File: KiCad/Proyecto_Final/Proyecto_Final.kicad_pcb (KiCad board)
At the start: 2 copper layers, 240 parts, among them J1 RF_IN, J10 PF, J11 PB, J12 PE, J13 PA, J14 PD, J15 SPI4, J16 CLK_SEL, J17 CTRL_MODE, J2 ADC_CLK_SEL, J3 5v, J4 I2C1, J5 ARM SWD, J6 USB_B_Micro, J7 Boot_Select, J8 PG, J9 PC, Q1 BSS315P, SW1 Reset, T1 B0310J50100AHF, T2 B0310J50100AHF, T3 2450BL05A0100, U1 SKY13351, U10 MAX2837, U11 TLV1117-33, U12 TPD4S012DRYR, U13 STM32F723ZCTx, U14 5P49V6975, U2 RFFC5072, U3 SKY13351, U4 SKY13351, U5 SKY13351, U6 SKY13351, U7 SKY13351, U8 MAAL-010200, U9 MAX1193ETI+, Y1 25MHz

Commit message: Avance PCB.
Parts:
- removed the R12 at (155.5, 47.4)
- removed the R13 at (158.4, 44.3)
- removed the R14 at (176.4, 60.3)
- removed the R15 at (152.6, 49.4)
- added R2: 10k, Resistor_SMD:R_0402_1005Metric, F.Cu at (78.7, 63.5)
- J16: value CLK_SEL -> CFG_SEL
- moved FB1 100.4 mm to (211.3, 86.4)
- moved D2 98.0 mm to (193.0, 115.6)
- moved L4 96.4 mm to (119.9, 131.3), turned to 270 degrees
- moved C58 95.9 mm to (118.3, 131.8), turned to 180 degrees
- moved C56 85.7 mm to (118.3, 130.9), turned to 180 degrees
- moved C2 74.1 mm to (105.7, 137.4), turned to 180 degrees
- moved C3 69.3 mm to (105.6, 128.7)
- moved C10 68.4 mm to (110.4, 129.5), turned to 270 degrees
- moved C8 68.1 mm to (102.9, 137.1), turned to 180 degrees
- moved C11 66.3 mm to (114.4, 131.6), turned to 180 degrees
- moved C4 62.2 mm to (105.6, 127.7)
- moved C1 61.9 mm to (105.7, 136.4), turned to 180 degrees
- moved C5 60.4 mm to (115.3, 129.5), turned to 90 degrees
- moved J17 60.2 mm to (113.0, 99.1)
- moved U1 59.9 mm to (113.9, 129.0), turned to 270 degrees
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- renumbered C14 to C13, C15 to C14, C16 to C15, C17 to C16, C13 to C17, R9 to R10, R10 to R11, R11 to R12, R16 to R13, R17 to R14, R18 to R15, R19 to R16, R20 to R17, R21 to R18, R22 to R19, R23 to R20, R24 to R21, R25 to R22, R34 to R23, R35 to R24, R26 to R25, R27 to R26, R28 to R27, R29 to R28, R30 to R29, R2 to R3, R31 to R30, R32 to R31, R33 to R32, R3 to R4, R4 to R5, R5 to R6, R6 to R7, R7 to R8, R8 to R9
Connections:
- net Net-(C56-Pad1) renamed /Transceptor/RXRF+
- net Net-(C58-Pad1) renamed /Transceptor/RXRF-
- net Net-(L1-Pad2) renamed /Frontend_analog/MIX_OPP
- net Net-(L2-Pad2) renamed /Frontend_analog/MIX_OPN
- T2 pad 3: MIX_IPP -> MIX_IPN
- T2 pad 4: MIX_IPN -> MIX_IPP
- T3 pad 3: Net-(C56-Pad2) -> Net-(C58-Pad2)
- T3 pad 4: Net-(C58-Pad2) -> Net-(C56-Pad2)
- U1 pad 1: Net-(C10-Pad1) -> SWITCH
- U1 pad 3: SWITCH -> Net-(C10-Pad1)
- U9 pad 1: _INA- -> INA-
- U9 pad 2: _INA+ -> INA+
- U9 pad 6: _INB+ -> INB+
- U9 pad 7: _INB- -> INB-
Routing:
- net GND: track 0.00 -> 9.33 mm, vias 0 -> 9
- net +3.3VA: track 0.00 -> 7.93 mm, vias 0 -> 2
- net /Frontend_analog/MIX_OPN: track 0.00 -> 6.96 mm
- net /Frontend_analog/MIX_OPP: track 0.00 -> 6.59 mm, vias 0 -> 2
- net Net-(C10-Pad1): track 0.00 -> 4.27 mm
- net /Transceptor/RXRF+: track 0.00 -> 4.11 mm
- net /Transceptor/RXRF-: track 0.00 -> 4.11 mm
- net VDD: track 0.00 -> 3.82 mm, vias 0 -> 1
- net SWITCH: track 0.00 -> 3.75 mm
- net Net-(C11-Pad2): track 0.00 -> 2.16 mm
- net Net-(C10-Pad2): track 0.00 -> 1.38 mm
- net Rx_Mix: track 0.00 -> 1.30 mm
- net Net-(C58-Pad2): track 0.00 -> 1.30 mm
- net Net-(C56-Pad2): track 0.00 -> 1.29 mm
- net Rx_Mix_Bypass: track 0.00 -> 1.23 mm
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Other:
- copper layers 2 -> 4
- net class 100 Ohms Diferencial added: clearance 0.1, trace_width 0.25, via_dia 0.6, via_drill 0.3
- net class 50 Ohms Unico added: clearance 0.1, trace_width 0.3, via_dia 0.6, via_drill 0.3
- net class 90 Ohms Diferencial added: clearance 0.1, trace_width 0.25, via_dia 0.6, via_drill 0.3
- net class Default: clearance 0.2 -> 0.1
- rule trace_clearance: 0.2 -> 0.1
- rule via_min_drill: 0.3 -> 0.2
- rule via_min_size: 0.4 -> 0.45

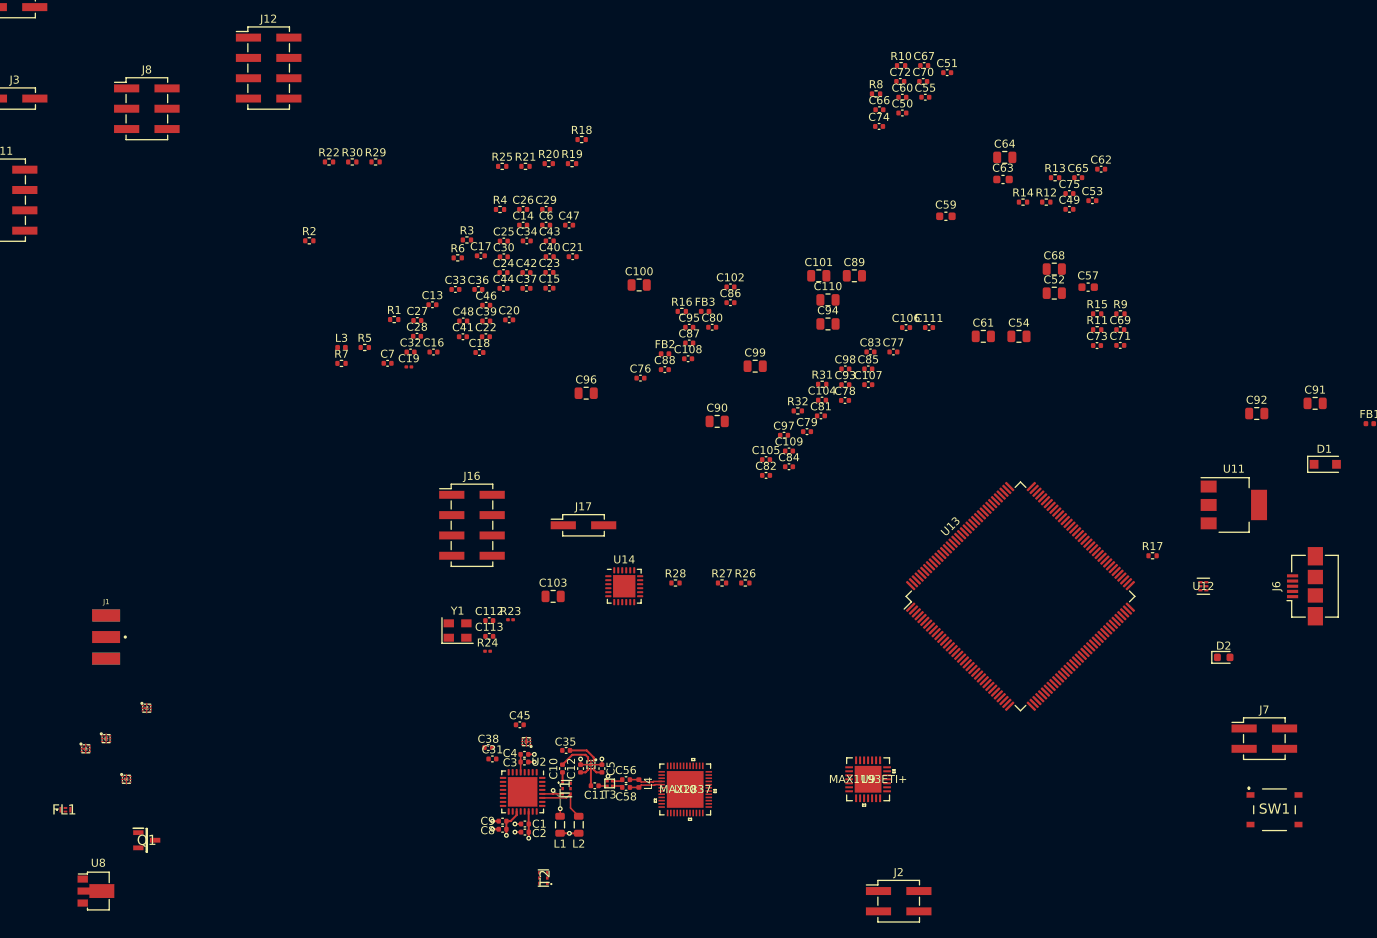
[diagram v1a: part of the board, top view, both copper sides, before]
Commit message: PCB Frontend terminado y empezado parte Transceptor.
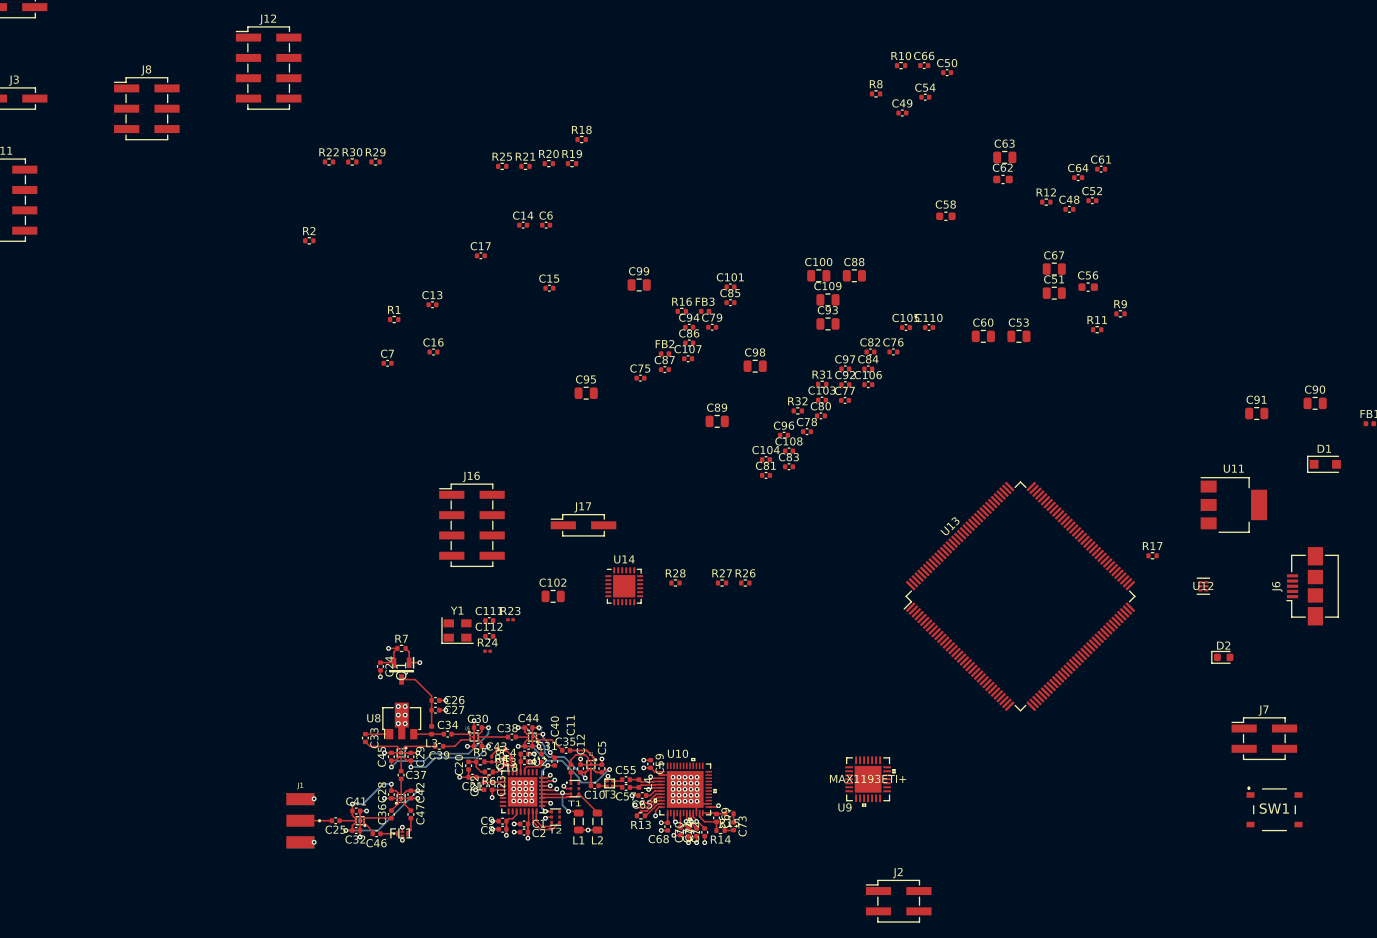
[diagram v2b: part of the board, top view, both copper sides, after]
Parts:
- removed the C44 at (103.0, 69.4)
- removed the C48 at (98.0, 73.5)
- removed the C60 at (152.9, 45.6)
- removed the C66 at (150.0, 47.1)
- removed the C72 at (152.6, 43.6)
- added C45: 33pF, Capacitor_SMD:C_0402_1005Metric, F.Cu at (89.0, 128.0)
- added C59: 22pF, Capacitor_SMD:C_0402_1005Metric, F.Cu at (121.4, 128.9)
- added C65: 22pF, Capacitor_SMD:C_0402_1005Metric, F.Cu at (120.4, 132.8)
- added C70: 10nF, Capacitor_SMD:C_0402_1005Metric, F.Cu at (126.1, 137.4)
- C41: value 100pF -> 33pF
- C46: value 33pF -> 100pF
- moved C69 95.6 mm to (129.6, 135.6), turned to 270 degrees
- moved R13 95.1 mm to (120.2, 135.4), turned to 180 degrees
- moved C74 93.4 mm to (125.1, 137.3), turned to 270 degrees
- moved C73 89.3 mm to (131.8, 136.7), turned to 270 degrees
- moved R14 87.2 mm to (130.1, 137.2), turned to 180 degrees
- moved C68 84.0 mm to (123.5, 136.7), turned to 270 degrees
- moved C71 80.7 mm to (127.2, 137.4), turned to 90 degrees
- moved C72 78.1 mm to (128.2, 137.4), turned to 90 degrees
- moved R15 77.6 mm to (131.3, 135.1), turned to 180 degrees
- moved C47 76.3 mm to (91.4, 135.2), turned to 270 degrees
- moved C25 75.4 mm to (82.0, 136.0), turned to 180 degrees
- moved C29 70.5 mm to (91.4, 128.0), turned to 90 degrees
- moved R4 67.5 mm to (102.8, 127.1), turned to 180 degrees
- moved C46 67.5 mm to (87.2, 137.6), turned to 180 degrees
- moved C42 66.8 mm to (91.4, 132.7), turned to 270 degrees
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- renumbered C11 to C10, C101 to C100, C102 to C101, C103 to C102, C104 to C103, C105 to C104, C106 to C105, C107 to C106, C108 to C107, C109 to C108, C110 to C109, C10 to C11, C111 to C110, C112 to C111, C113 to C112, C45 to C44, C49 to C48, C50 to C49, C51 to C50, C52 to C51, C53 to C52, C54 to C53, C55 to C54, C56 to C55, C57 to C56, C58 to C57, C59 to C58, C61 to C60, C62 to C61, C63 to C62, C64 to C63, C65 to C64, C67 to C66, C68 to C67, C69 to C68, C70 to C69, C73 to C72, C74 to C73, C75 to C74, C76 to C75, C77 to C76, C78 to C77, C79 to C78, C80 to C79, C81 to C80, C82 to C81, C83 to C82, C84 to C83, C85 to C84, C86 to C85, C87 to C86, C88 to C87, C89 to C88, C90 to C89, C91 to C90, C92 to C91, C93 to C92, C94 to C93, C95 to C94, C96 to C95, C97 to C96, C98 to C97, C99 to C98, C100 to C99
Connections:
- C12 pad 1: Rx_Mix_Bypass -> Rx_Mix
- C29 pad 1: Rx_Amp -> Rx_Amp_Bypass
- C32 pad 1: Filt_Bypass -> Filtro
- C40 pad 2: Net-(C39-Pad1) -> Net-(C40-Pad2)
- C41 pad 1: Net-(C41-Pad1) -> Filt_Bypass
- C41 pad 2: Net-(C41-Pad2) -> GND
- C43 pad 1: Filtro -> Rx_Amp_Bypass
- C46 pad 1: Rx_Amp_Bypass -> Net-(C46-Pad1)
- C46 pad 2: GND -> Net-(C46-Pad2)
- C5 pad 1: Rx_Mix -> Rx_Mix_Bypass
- FL1 pad 1: Net-(C47-Pad1) -> Net-(C46-Pad1)
- FL1 pad 3: Net-(C48-Pad2) -> Net-(C47-Pad2)
- T2 pad 1: Net-(C41-Pad1) -> Net-(C40-Pad1)
- U1 pad 4: Rx_Mix_Bypass -> Rx_Mix
- U1 pad 6: Rx_Mix -> Rx_Mix_Bypass
- U3 pad 1: Net-(C36-Pad2) -> Net-(C46-Pad2)
- U3 pad 3: Net-(C47-Pad2) -> Net-(C36-Pad2)
- U3 pad 4: Filtro -> Filt_Bypass
- U3 pad 6: Filt_Bypass -> Filtro
- U4 pad 3: Net-(C48-Pad1) -> Net-(C47-Pad1)
- U5 pad 1: Net-(C33-Pad2) -> Net-(C39-Pad2)
- U5 pad 3: Net-(C39-Pad2) -> Net-(C33-Pad2)
- U5 pad 4: Rx_Amp_Bypass -> Rx_Amp
- U5 pad 6: Rx_Amp -> Rx_Amp_Bypass
- U6 pad 3: Net-(C40-Pad1) -> Net-(C39-Pad1)
- U7 pad 3: Net-(C41-Pad2) -> Net-(C40-Pad2)
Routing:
- net GND: track 9.33 -> 56.6 mm, vias 9 -> 83
- net Rx_Amp: track 0.00 -> 18.5 mm, vias 0 -> 2
- net VDD: track 3.82 -> 22.2 mm, vias 1 -> 7
- net Rx_Mix_Bypass: track 1.23 -> 18.5 mm, vias 0 -> 2
- net Filtro: track 0.00 -> 15.1 mm, vias 0 -> 2
- net Rx_Amp_Bypass: track 0.00 -> 14.7 mm, vias 0 -> 2
- net Rx_Mix: track 1.30 -> 15.4 mm, vias 0 -> 2
- net Filt_Bypass: track 0.00 -> 9.91 mm, vias 0 -> 2
- net Net-(C26-Pad1): track 0.00 -> 8.41 mm
- net Net-(C40-Pad1): track 0.00 -> 7.93 mm, vias 0 -> 2
- net LFILT3: track 0.00 -> 5.52 mm
- net MIX_IPP: track 0.00 -> 5.42 mm
- net LFILT2: track 0.00 -> 5.00 mm
- net Net-(C33-Pad2): track 0.00 -> 4.59 mm
- net Net-(C40-Pad2): track 0.00 -> 4.39 mm, vias 0 -> 2
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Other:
- net class 100 Ohms Diferencial: trace_width 0.25 -> 0.2
- net class 90 Ohms Diferencial: trace_width 0.25 -> 0.2
- net class Default: trace_width 0.25 -> 0.2; via_dia 0.8 -> 0.6; via_drill 0.4 -> 0.3

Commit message: PCB Transceptor 95%.
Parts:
- moved C66 94.7 mm to (131.2, 133.1), turned to 180 degrees
- moved C50 89.7 mm to (128.2, 126.9), turned to 225 degrees
- moved R10 86.6 mm to (122.6, 122.8), turned to 180 degrees
- moved C61 85.5 mm to (136.6, 129.5), turned to 90 degrees
- moved R12 84.3 mm to (119.5, 125.6), turned to 180 degrees
- moved C63 84.2 mm to (142.3, 134.0)
- moved C49 84.1 mm to (123.8, 126.5), turned to 270 degrees
- moved C64 82.8 mm to (137.6, 129.5), turned to 90 degrees
- moved C52 82.1 mm to (135.5, 129.5), turned to 90 degrees
- moved R8 82.0 mm to (126.8, 124.0)
- moved C48 81.6 mm to (126.3, 125.9), turned to 270 degrees
- moved C67 77.9 mm to (133.9, 135.0), turned to 90 degrees
- moved C54 77.7 mm to (134.9, 120.3), turned to 180 degrees
- moved R11 74.0 mm to (122.1, 124.0), turned to 180 degrees
- moved R9 73.6 mm to (126.3, 122.8)
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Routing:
- net SPI1_MOSI: track 1.14 -> 45.1 mm, vias 1 -> 2
- net SPI1_MISO: track 1.13 -> 39.0 mm, vias 1 -> 2
- net SPI1_CS0: track 1.01 -> 38.5 mm
- net GND: track 56.6 -> 88.8 mm, vias 83 -> 115
- net Trx_Rx_Enable: track 0.00 -> 27.4 mm, vias 0 -> 1
- net VDD: track 22.2 -> 48.1 mm, vias 7 -> 18
- net SPI1_SCK: track 2.85 -> 22.6 mm, vias 2 -> 3
- net RXHP: track 0.00 -> 18.7 mm, vias 0 -> 1
- net B6: track 0.00 -> 15.4 mm, vias 0 -> 1
- net B7: track 0.00 -> 14.4 mm, vias 0 -> 1
- net RSSI: track 0.00 -> 14.4 mm, vias 0 -> 1
- net B5: track 1.44 -> 15.1 mm
- net RESETX: track 1.90 -> 15.3 mm
- net B2: track 3.98 -> 16.9 mm
- net B4: track 1.71 -> 14.5 mm
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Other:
- board outline added: 102 x 102 mm

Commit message: PCB MCU empezado.
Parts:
- removed the C94 at (126.2, 74.3)
- removed the C95 at (113.3, 82.5)
- removed the R23 at (103.9, 110.9)
- removed the R24 at (101.0, 114.8)
- added J16: OutEn, Connector_PinHeader_2.54mm:PinHeader_2x02_P2.54mm_Vertical_SMD, F.Cu at (109.9, 113.2)
- added R13: 10k, Resistor_SMD:R_0402_1005Metric, F.Cu at (127.0, 111.9)
- added R27: 10k, Resistor_SMD:R_0402_1005Metric, F.Cu at (117.9, 112.4)
- C101: renamed from C103; value 0.1uF -> 100nF
- C102: renamed from C104; value 0.1uF -> 100nF
- C103: renamed from C105; value 0.1uF -> 100nF
- C104: renamed from C106; value 0.1uF -> 100nF
- C105: renamed from C107; value 0.1uF -> 100nF
- C106: renamed from C108; value 0.1uF -> 100nF
- C108: renamed from C110; value 0.1uF -> 100nF
- C24: value 0.1uF -> 100nF
- C27: value 0.1uF -> 1uF; footprint Capacitor_SMD:C_0402_1005Metric -> Capacitor_SMD:C_0805_2012Metric
- U14: value 5P49V6975 -> 5P49V5929
- moved C97 70.4 mm to (166.9, 121.5), turned to 270 degrees
- moved FB2 64.0 mm to (186.4, 87.8)
- moved C85 59.2 mm to (163.0, 121.3), turned to 270 degrees
- moved R21 58.3 mm to (151.0, 94.0)
- moved C86 55.0 mm to (157.8, 121.3), turned to 270 degrees
- moved C96 53.9 mm to (172.8, 117.2), turned to 270 degrees
- moved C87 48.6 mm to (150.1, 120.1), turned to 180 degrees
- moved C89 48.3 mm to (173.1, 107.3)
- moved C94 46.6 mm to (184.7, 86.4)
- moved C84 45.6 mm to (169.6, 120.0)
- moved C98 45.0 mm to (173.1, 100.8)
- moved C95 42.5 mm to (187.7, 86.1)
- moved C75 42.1 mm to (146.7, 113.4), turned to 180 degrees
- moved C93 40.5 mm to (144.0, 114.4), turned to 90 degrees
- moved C83 38.7 mm to (172.7, 110.2)
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- renumbered C102 to C100, C109 to C107, C111 to C109, C112 to C110, C96 to C94, C97 to C95, C98 to C96, C99 to C97, C100 to C98, C101 to C99, J16 to J17, J17 to J18, R13 to R14, R14 to R15, R15 to R16, R16 to R17, R17 to R18, R18 to R19, R19 to R20, R20 to R21, R21 to R22, R22 to R23, R25 to R24, R26 to R25, R27 to R26
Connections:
- net USB_OTG_HS_DM renamed USB_OTG_HS_D-
- net USB_OTG_HS_DP renamed USB_OTG_HS_D+
- U13 pad 48: PD1 -> PD0_adc
- U13 pad 49: PD0 -> PD1_adc
- U13 pad 50: A_B -> D0
- U13 pad 53: D0 -> D1
- U13 pad 54: D1 -> D2
- U13 pad 55: D2 -> D3
- U13 pad 56: D3 -> A_B
- U14 pad 3: Net-(R23-Pad1) -> XOUT
- U14 pad 4: Net-(R24-Pad1) (its old number) -> XIN
- U14 pad 7: Net-(U14-Pad7) -> SD_OE
- U9 pad 22: PD1 -> PD1_adc
- U9 pad 23: PD0 -> PD0_adc
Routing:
- net VDD: track 48.1 -> 81.4 mm, vias 18 -> 31
- net D7: track 0.00 -> 30.7 mm
- net D6: track 0.00 -> 29.3 mm
- net D5: track 0.00 -> 26.0 mm
- net D4: track 0.00 -> 24.7 mm
- net A_B: track 0.00 -> 23.9 mm
- net D3: track 0.00 -> 23.0 mm
- net D2: track 0.00 -> 22.1 mm
- net D1: track 0.00 -> 21.2 mm
- net PD0_adc: track 0.00 -> 20.3 mm
- net PD1_adc: track 0.00 -> 20.2 mm
- net D0: track 0.00 -> 19.5 mm
- net GND: track 88.8 -> 107.5 mm, vias 115 -> 163
- net USB_OTG_HS_D+: track 0.00 -> 17.4 mm
- net USB_OTG_HS_D-: track 0.00 -> 16.7 mm
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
